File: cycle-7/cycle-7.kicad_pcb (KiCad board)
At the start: 2 copper layers, 347.7 x 94.2 mm, 179 parts, among them J1 Conn_01x06_MountingPin, J2 Conn_01x04_Pin, J3 Conn_01x02_Pin, SW1 SW_Push, U1 XC6206PxxxMR, U2 STM32F401RCTx, U3 SRV05-4, Y1 12MHz

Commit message: added a readme, fixed kicad update mess..
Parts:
- C11: value 4.7u -> 100n
- J1: footprint Connector_JST:JST_SHL_SM06B-SHLS-TF_1x06-1MP_P1.00mm_Horizontal -> Connector_JST:JST_SH_SM06B-SRSS-TB_1x06-1MP_P1.00mm_Horizontal
- R1, R2: value 27 -> 0
- renumbered D14 to D13, D15 to D14, D16 to D15, D17 to D16, D18 to D17, D19 to D18, D20 to D19, D21 to D20, D22 to D21, D23 to D22, D24 to D23, D25 to D24, D26 to D25, D27 to D26, D28 to D27, D29 to D28, D31 to D29, D32 to D30, D33 to D31, D34 to D32, D35 to D33, D36 to D34, D37 to D35, D38 to D36, D39 to D37, D40 to D38, D41 to D39, D42 to D40, D43 to D41, D44 to D42, D45 to D43, D46 to D44, D13 to D45, D47 to D46, D48 to D47, D49 to D48, D50 to D49, D51 to D50, D52 to D51, D53 to D52, D54 to D53, D55 to D54, D56 to D55, D57 to D56, D58 to D57, D30 to D58, J3 to J2, J2 to J3, MX14 to MX13, MX15 to MX14, MX16 to MX15, MX17 to MX16, MX18 to MX17, MX19 to MX18, MX20 to MX19, MX21 to MX20, MX22 to MX21, MX23 to MX22, MX24 to MX23, MX25 to MX24, MX26 to MX25, MX27 to MX26, MX28 to MX27, MX29 to MX28, MX31 to MX29, MX32 to MX30, MX33 to MX31, MX34 to MX32, MX35 to MX33, MX36 to MX34, MX37 to MX35, MX38 to MX36, MX39 to MX37, MX40 to MX38, MX41 to MX39, MX42 to MX40, MX43 to MX41, MX44 to MX42, MX45 to MX43, MX46 to MX44, MX13 to MX45, MX47 to MX46, MX48 to MX47, MX49 to MX48, MX50 to MX49, MX51 to MX50, MX52 to MX51, MX53 to MX52, MX54 to MX53, MX55 to MX54, MX56 to MX55, MX57 to MX56, MX58 to MX57, MX30 to MX58, R5 to R4, R4 to R5, S6 to S5, S5 to S6, U3 to U2, U2 to U3
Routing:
- net +5V: track 199.6 -> 200.6 mm
- net GND: track 30.4 -> 31.0 mm
- net /USB_D+: track 162.1 -> 162.7 mm

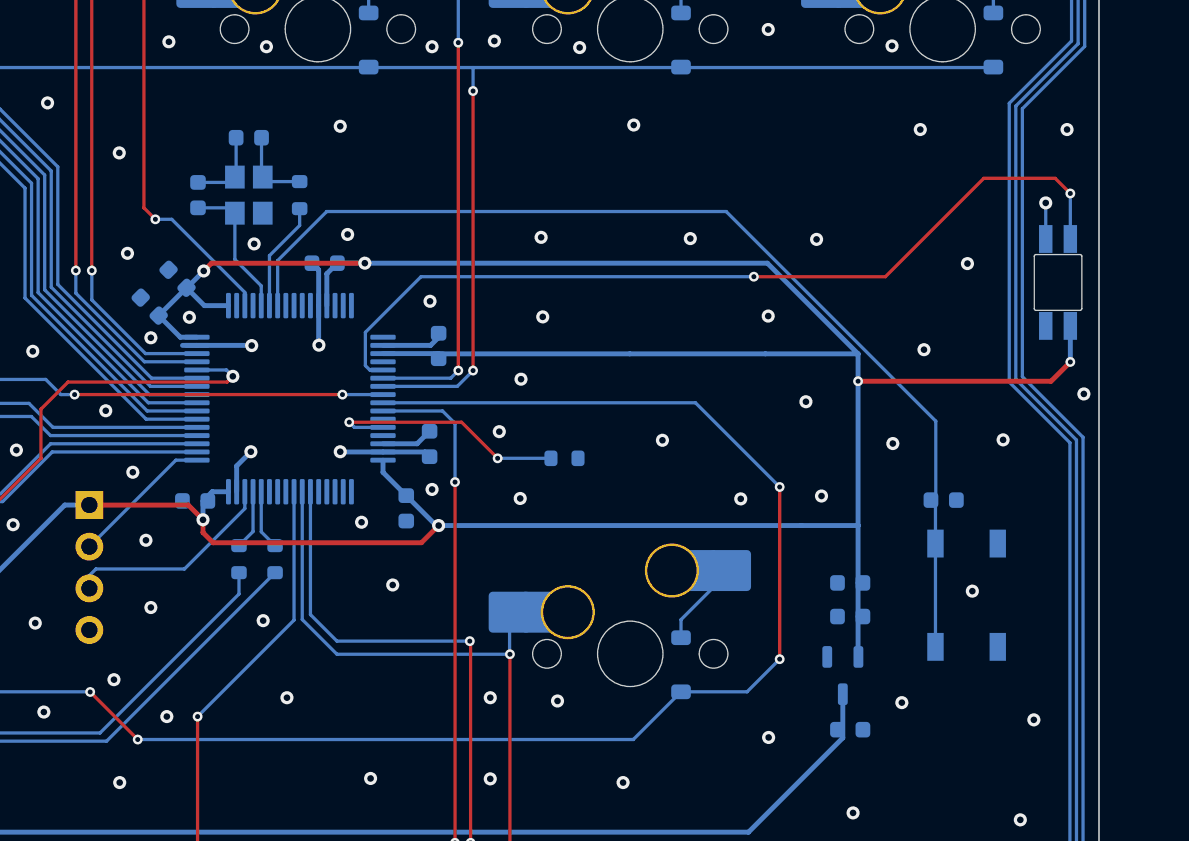
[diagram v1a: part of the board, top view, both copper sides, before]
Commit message: updated findings from prototype removed output folder as the vendors stock is everchanging
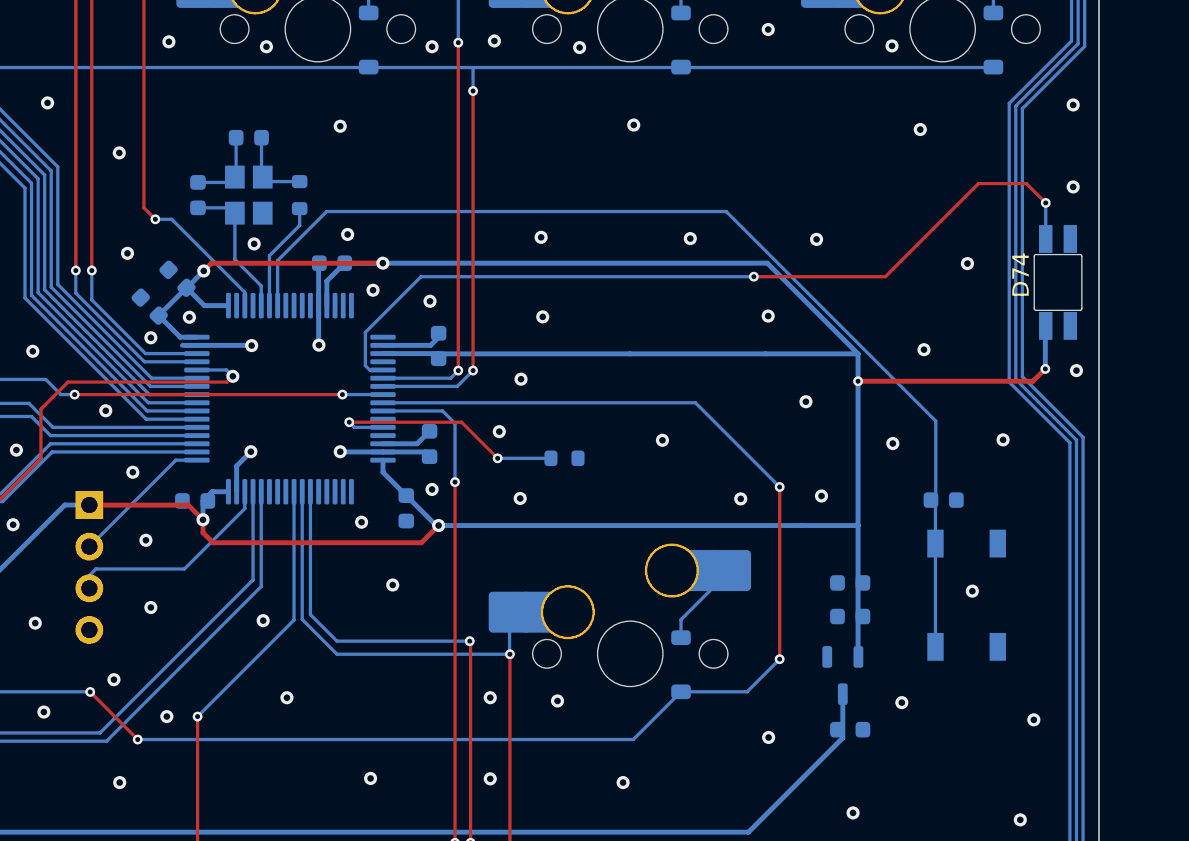
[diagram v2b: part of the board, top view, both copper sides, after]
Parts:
- removed R1, R2: 0, Resistor_SMD:R_0603_1608Metric
- D74: moved to F.Cu
- moved C4 0.45 mm to (331.4, 123.3)
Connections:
- U3 pad 44: Net-(U3-PA11) -> /USB_D-
- U3 pad 45: Net-(U3-PA12) -> /USB_D+
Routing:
- net /USB_D+: track 162.7 -> 168.0 mm
- net /USB_D-: track 162.9 -> 167.5 mm
- net Net-(U3-PA12): track 3.64 -> 0.00 mm
- net Net-(U3-PA11): track 3.64 -> 0.00 mm
- net GND: track 31.0 -> 28.7 mm, vias 396 -> 397
- net /LED_SIG: track 53.3 -> 51.1 mm
